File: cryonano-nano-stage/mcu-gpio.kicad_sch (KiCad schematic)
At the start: 18 parts, among them U11 STM32H753ZITx

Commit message: sch improved
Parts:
- removed C14: 4.7u, Capacitor_SMD:C_0603_1608Metric, symbol Device:C_Small
- removed C15, C43, C44, C45, C46, C47, C48, C49, C50, C53, C55: 100n, Capacitor_SMD:C_0603_1608Metric, symbol Device:C_Small
- removed C51, C52, C54: 1u, Capacitor_SMD:C_0603_1608Metric, symbol Device:C_Small
- removed C56, C57: 2.2u, Capacitor_SMD:C_0603_1608Metric, symbol Device:C_Small
- removed U11: STM32H753ZITx, Package_QFP:LQFP-144_20x20mm_P0.5mm, symbol symbols:STM32H753ZITx
- added C16, C17: 100n, Capacitor_SMD:C_0603_1608Metric, symbol Device:C_Small
- added C33, C34, C36, C37: 22pF, Capacitor_SMD:C_0603_1608Metric, symbol Device:C_Small
- added D1: PESD3V3S1UL, Diode_SMD:D_SOD-882, symbol Diode:PESD3V3S1UL
- added R35: 470R, Resistor_SMD:R_0603_1608Metric, symbol Device:R_Small
- added R36, R38, R68, R86: 10k, Resistor_SMD:R_0603_1608Metric, symbol Device:R_Small
- added SW1: BOOT, Button_Switch_THT:SW_PUSH_6mm, symbol Switch:SW_Push
- added SW2: RESET, Button_Switch_THT:SW_PUSH_6mm, symbol Switch:SW_Push
- added U11: STM32H753ZITx, Package_QFP:LQFP-144_20x20mm_P0.5mm, symbol symbols:STM32H753ZITx
- added Y2, Y4: 12.0MHz, Crystal:Crystal_SMD_3215-2Pin_3.2x1.5mm, symbol Device:Crystal
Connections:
- net VDD: now also R35.1, R38.1
- new net: R35.2, SW1.2
- new net BOOT0: C16.1, R36.1, SW1.1, U11.138 (BOOT0)
- new net CLKOUT: U11.100 (PA8)
- new net LOG_RX: U11.112 (PC11)
- new net LOG_TX: U11.111 (PC10)
- new net NRST: C17.1, D1.1 (K), SW2.1, U11.25 (NRST)
- new net PA0: U11.34 (PA0)
- new net PA15: U11.110 (PA15)
- new net PA3: U11.37 (PA3)
- new net PA4: U11.40 (PA4)
- new net PA5: U11.41 (PA5)
- new net PA6: U11.42 (PA6)
- new net PA9: R68.2, U11.101 (PA9)
- new net PB0: U11.46 (PB0)
- new net PB1: U11.47 (PB1)
- new net PB11: U11.70 (PB11)
- new net PB12: U11.73 (PB12)
- new net PB2: U11.48 (PB2)
- new net PB4: U11.134 (PB4)
- new net PB5: U11.135 (PB5)
- new net PB6: U11.136 (PB6)
- new net PB7: U11.137 (PB7)
- new net PB8: U11.139 (PB8)
- new net PB9: U11.140 (PB9)
- new net PC0: U11.26 (PC0)
- new net PC12: U11.113 (PC12)
- new net PC13: U11.7 (PC13)
- new net PC2: U11.28 (PC2_C)
- new net PC3: U11.29 (PC3_C)
- new net PC6: U11.96 (PC6)
- new net PC7: U11.97 (PC7)
- new net PC8: U11.98 (PC8)
- new net PC9: U11.99 (PC9)
- new net PD0: U11.114 (PD0)
- new net PD1: U11.115 (PD1)
- new net PD12: U11.81 (PD12)
- new net PD13: U11.82 (PD13)
- new net PD14: U11.85 (PD14)
- new net PD15: U11.86 (PD15)
- new net PD2: U11.116 (PD2)
- new net PD3: U11.117 (PD3)
- new net PD4: U11.118 (PD4)
- new net PD5: U11.119 (PD5)
- new net PD6: U11.122 (PD6)
- new net PD7: U11.123 (PD7)
- new net PD8: U11.77 (PD8)
- new net PD9: U11.78 (PD9)
- new net PDR_ON: R38.2, R86.1, U11.143 (PDR_ON)
- new net PE0: U11.141 (PE0)
- new net PE1: U11.142 (PE1)
- new net PE10: U11.63 (PE10)
- new net PE11: U11.64 (PE11)
- new net PE12: U11.65 (PE12)
- new net PE13: U11.66 (PE13)
- new net PE14: U11.67 (PE14)
- new net PE2: U11.1 (PE2)
- new net PE3: U11.2 (PE3)
- new net PE4: U11.3 (PE4)
- new net PE5: U11.4 (PE5)
- new net PE6: U11.5 (PE6)
- new net PE7: U11.58 (PE7)
- new net PE8: U11.59 (PE8)
- new net PF0: U11.10 (PF0)
- new net PF1: U11.11 (PF1)
- new net PF10: U11.22 (PF10)
- new net PF11: U11.49 (PF11)
- new net PF12: U11.50 (PF12)
- new net PF13: U11.53 (PF13)
- new net PF14: U11.54 (PF14)
- new net PF15: U11.55 (PF15)
- new net PF2: U11.12 (PF2)
- new net PF3: U11.13 (PF3)
- new net PF4: U11.14 (PF4)
- new net PF5: U11.15 (PF5)
- new net PF6: U11.18 (PF6)
- new net PF7: U11.19 (PF7)
- new net PF8: U11.20 (PF8)
- new net PF9: U11.21 (PF9)
- new net PG0: U11.56 (PG0)
- new net PG1: U11.57 (PG1)
- new net PG10: U11.125 (PG10)
- new net PG12: U11.127 (PG12)
- new net PG14: U11.129 (PG14)
- new net PG15: U11.132 (PG15)
- new net PG2: U11.87 (PG2)
- new net PG3: U11.88 (PG3)
- new net PG4: U11.89 (PG4)
- new net PG5: U11.90 (PG5)
- new net PG6: U11.91 (PG6)
- new net PG7: U11.92 (PG7)
- new net PG8: U11.93 (PG8)
- new net PG9: U11.124 (PG9)
- new net PWMOUT: U11.60 (PE9)
- new net RCC_OSC32_IN: C36.1, U11.8 (PC14), Y2.2
- new net RCC_OSC32_OUT: C37.1, U11.9 (PC15), Y2.1
- new net RCC_OSC_IN: C33.1, U11.23 (PH0), Y4.2
- new net RCC_OSC_OUT: C34.1, U11.24 (PH1), Y4.1
- new net RMII_CRS_DV: U11.43 (PA7)
- new net RMII_MDC: U11.27 (PC1)
- new net RMII_MDIO: U11.36 (PA2)
- new net RMII_REF_CLK: U11.35 (PA1)
- new net RMII_RXD0: U11.44 (PC4)
- new net RMII_RXD1: U11.45 (PC5)
- new net RMII_TXD0: U11.128 (PG13)
- new net RMII_TXD1: U11.74 (PB13)
- new net RMII_TX_EN: U11.126 (PG11)
- new net SCK: U11.69 (PB10)
- new net SDI: U11.76 (PB15)
- new net SDO/~{IRQ}: U11.75 (PB14), U11.79 (PD10)
- new net SWCLK: U11.109 (PA14)
- new net SWDIO: U11.105 (PA13)
- new net SWO: U11.133 (PB3)
- new net USB_D+: U11.104 (PA12)
- new net USB_D-: U11.103 (PA11)
- new net USB_ID: U11.102 (PA10)
- new net USB_VBUS_SENSE: R68.1
- new net VSS: C16.2, C17.2, C33.2, C34.2, C36.2, C37.2, D1.2 (A), R36.2, R86.2, SW2.2
- new net ~{CS}: U11.80 (PD11)
- new net ~{SYNC}: U11.68 (PE15)
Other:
- note added: "BOOT memory selection."
- note added: "RESET"

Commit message: pcb drc ok. 68 ohm matching pending
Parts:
- removed D1: PESD3V3S1UL, Diode_SMD:D_SOD-882, symbol Diode:PESD3V3S1UL
- added D6: ESDB3V3C-AQ, symbol symbols:ESDB3V3C-AQ
- added TP2: TEST POINT, footprints:TestPoint_THTPad_D1.3mm_Drill0.8mm, symbol Connector:TestPoint
- added TP3: 1x02 2.54mm, Connector_PinSocket_2.54mm:PinSocket_1x02_P2.54mm_Vertical, symbol Connector:Conn_01x02_Socket
- C16: Manufacturer (none) -> KEMET; Order No. (none) -> C0603C104K5RAC7411; Unit Price 10 (none) -> 2.5
- C17: Manufacturer (none) -> KEMET; Order No. (none) -> C0603C104K5RAC7411; Tolerence 10% -> (none); Unit Price 10 (none) -> 2.5
- C33, C34, C36, C37: Manufacturer (none) -> YAGEO; Manufacturer_Name SAMSUNG ELECTRO-MECHANICS -> (none); Order No. (none) -> CC0603JPNPO9BN220; Unit Price 10 (none) -> 2.3; Voltage 50V -> 16V
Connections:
- net PB11 is gone; now on net RMII_TX_EN: U11.70 (PB11)
- net PB12 is gone; now on net RMII_TXD0: U11.73 (PB12)
- net PC9 is gone; now on net CLKOUT: U11.99 (PC9)
- net PE10 is gone; now on net SDO/~{IRQ}: U11.63 (PE10)
- net PE11 is gone; now on net ~{CS}: U11.64 (PE11)
- net PE12 is gone; now on net SCK: U11.65 (PE12)
- net PE13 is gone; now on net SDO/~{IRQ}: U11.66 (PE13)
- net PE14 is gone; now on net SDI: U11.67 (PE14)
- net BOOT0: now also D6.2 (SIG2)
- net CLKOUT: no longer U11.100 (PA8)
- net NRST: now also D6.1 (SIG1)
- net PB6: now also TP3.1 (Pin_1)
- net PB7: now also TP3.2 (Pin_2)
- net RMII_TXD0: no longer U11.128 (PG13)
- net RMII_TX_EN: no longer U11.126 (PG11)
- net SCK: no longer U11.69 (PB10)
- net SDI: no longer U11.76 (PB15)
- net SDO/~{IRQ}: no longer U11.75 (PB14), U11.79 (PD10)
- net VSS: now also D6.3 (COM)
- net ~{CS}: no longer U11.80 (PD11)
- new net PA8: TP2.1, U11.100 (PA8)
- new net PB10: U11.69 (PB10)
- new net PB14: U11.75 (PB14)
- new net PB15: U11.76 (PB15)
- new net PD10: U11.79 (PD10)
- new net PD11: U11.80 (PD11)
- new net PG11: U11.126 (PG11)
- new net PG13: U11.128 (PG13)
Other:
- note added: "ESD"
- moved on the sheet: C16, C17, R35, R36, SW1, SW2

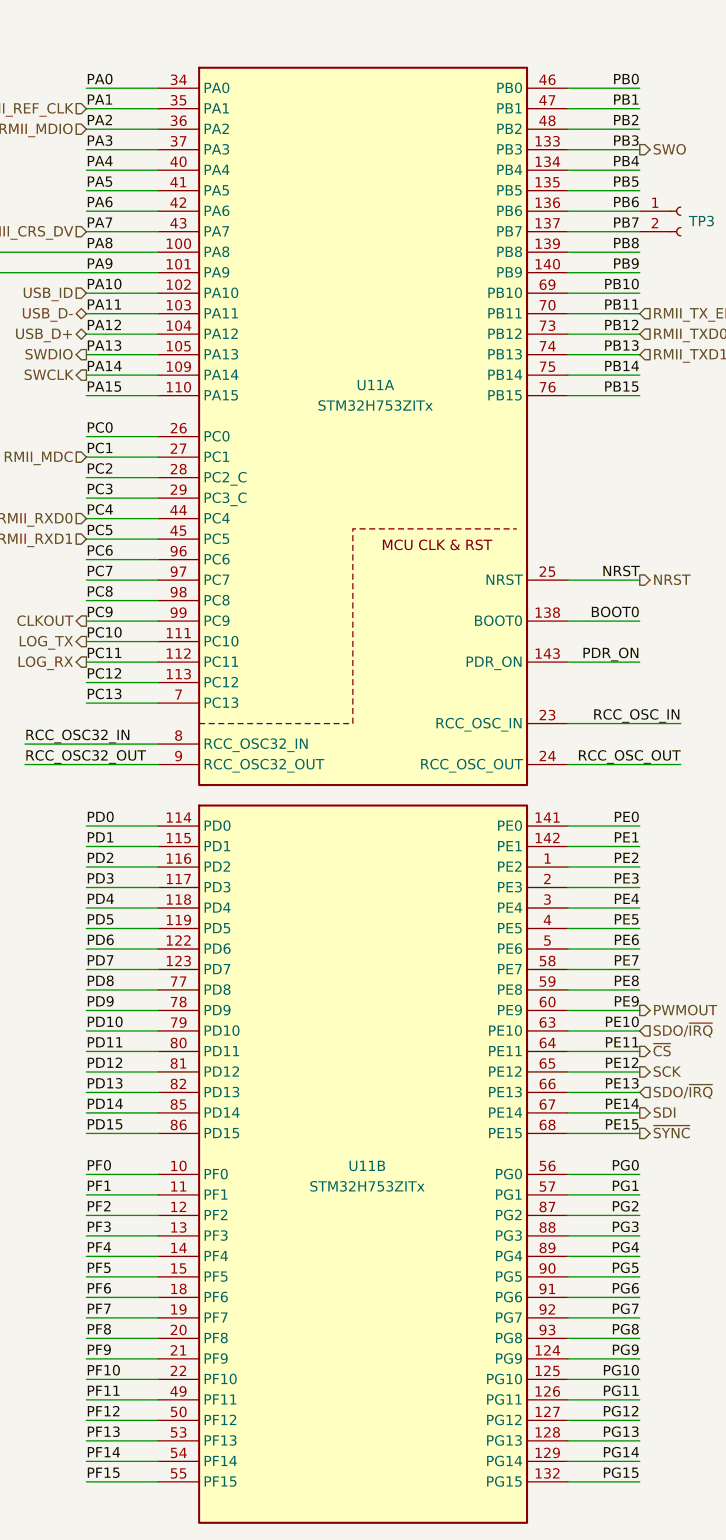
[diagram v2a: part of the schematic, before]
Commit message: drc no error, only warnings
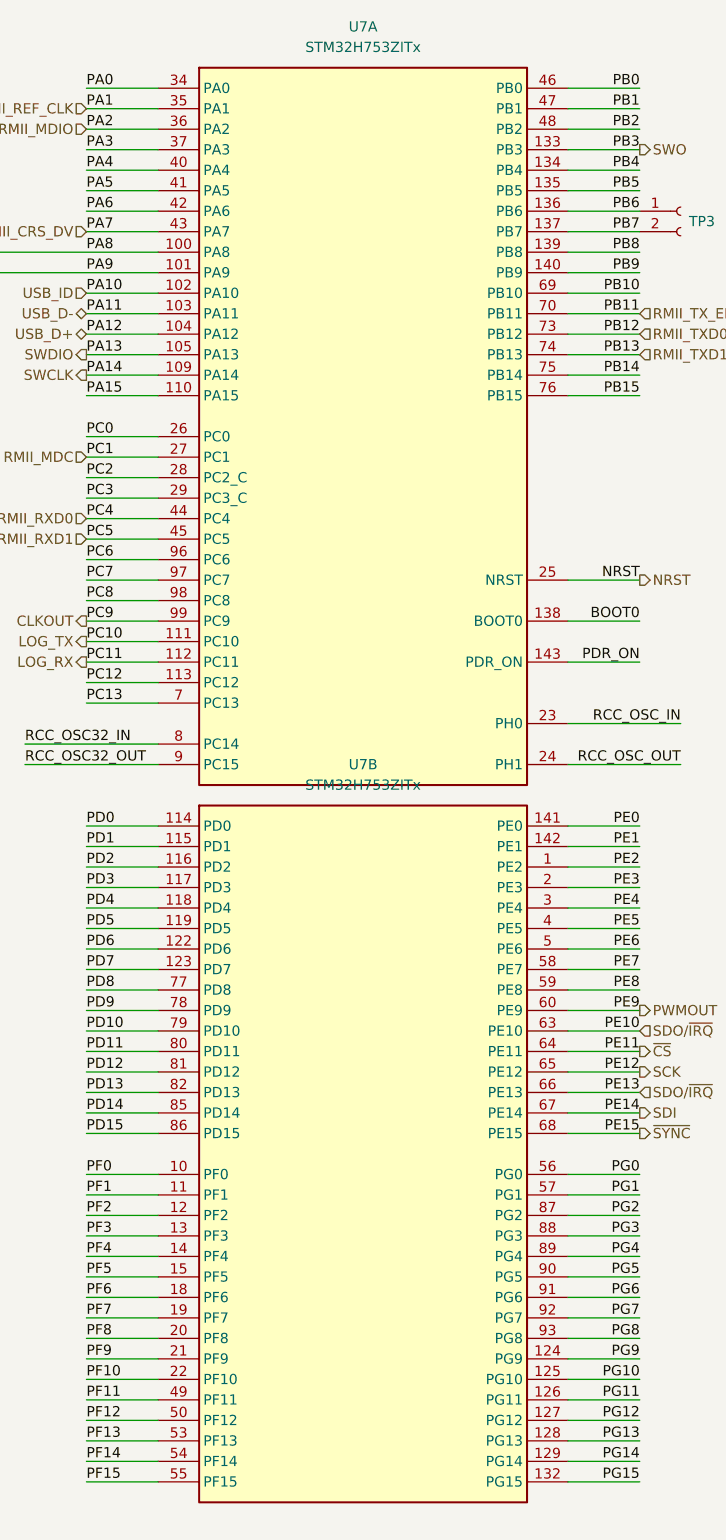
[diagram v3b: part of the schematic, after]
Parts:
- removed U11: STM32H753ZITx, Package_QFP:LQFP-144_20x20mm_P0.5mm, symbol symbols:STM32H753ZITx
- added U7: STM32H753ZITx, Package_QFP:LQFP-144_20x20mm_P0.5mm, symbol symbols:STM32H753ZITx
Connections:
- net BOOT0: now also U7.138 (BOOT0)
- net CLKOUT: now also U7.99 (PC9)
- net LOG_RX: now also U7.112 (PC11)
- net LOG_TX: now also U7.111 (PC10)
- net NRST: now also U7.25 (NRST)
- net PA0: now also U7.34 (PA0)
- net PA15: now also U7.110 (PA15)
- net PA3: now also U7.37 (PA3)
- net PA4: now also U7.40 (PA4)
- net PA5: now also U7.41 (PA5)
- net PA6: now also U7.42 (PA6)
- net PA8: now also U7.100 (PA8)
- net PA9: now also U7.101 (PA9)
- net PB0: now also U7.46 (PB0)
- net PB1: now also U7.47 (PB1)
- net PB10: now also U7.69 (PB10)
- net PB14: now also U7.75 (PB14)
- net PB15: now also U7.76 (PB15)
- net PB2: now also U7.48 (PB2)
- net PB4: now also U7.134 (PB4)
- net PB5: now also U7.135 (PB5)
- net PB6: now also U7.136 (PB6)
- net PB7: now also U7.137 (PB7)
- net PB8: now also U7.139 (PB8)
- net PB9: now also U7.140 (PB9)
- net PC0: now also U7.26 (PC0)
- net PC12: now also U7.113 (PC12)
- net PC13: now also U7.7 (PC13)
- net PC2: now also U7.28 (PC2_C)
- net PC3: now also U7.29 (PC3_C)
- net PC6: now also U7.96 (PC6)
- net PC7: now also U7.97 (PC7)
- net PC8: now also U7.98 (PC8)
- net PD0: now also U7.114 (PD0)
- net PD1: now also U7.115 (PD1)
- net PD10: now also U7.79 (PD10)
- net PD11: now also U7.80 (PD11)
- net PD12: now also U7.81 (PD12)
- net PD13: now also U7.82 (PD13)
- net PD14: now also U7.85 (PD14)
- net PD15: now also U7.86 (PD15)
- net PD2: now also U7.116 (PD2)
- net PD3: now also U7.117 (PD3)
- net PD4: now also U7.118 (PD4)
- net PD5: now also U7.119 (PD5)
- net PD6: now also U7.122 (PD6)
- net PD7: now also U7.123 (PD7)
- net PD8: now also U7.77 (PD8)
- net PD9: now also U7.78 (PD9)
- net PDR_ON: now also U7.143 (PDR_ON)
- net PE0: now also U7.141 (PE0)
- net PE1: now also U7.142 (PE1)
- net PE2: now also U7.1 (PE2)
- net PE3: now also U7.2 (PE3)
- net PE4: now also U7.3 (PE4)
- net PE5: now also U7.4 (PE5)
- net PE6: now also U7.5 (PE6)
- net PE7: now also U7.58 (PE7)
- net PE8: now also U7.59 (PE8)
- net PF0: now also U7.10 (PF0)
- net PF1: now also U7.11 (PF1)
- net PF10: now also U7.22 (PF10)
- net PF11: now also U7.49 (PF11)
- net PF12: now also U7.50 (PF12)
- net PF13: now also U7.53 (PF13)
- net PF14: now also U7.54 (PF14)
- net PF15: now also U7.55 (PF15)
- net PF2: now also U7.12 (PF2)
- net PF3: now also U7.13 (PF3)
- net PF4: now also U7.14 (PF4)
- net PF5: now also U7.15 (PF5)
- net PF6: now also U7.18 (PF6)
- net PF7: now also U7.19 (PF7)
- net PF8: now also U7.20 (PF8)
- net PF9: now also U7.21 (PF9)
- net PG0: now also U7.56 (PG0)
- net PG1: now also U7.57 (PG1)
- net PG10: now also U7.125 (PG10)
- net PG11: now also U7.126 (PG11)
- net PG12: now also U7.127 (PG12)
- net PG13: now also U7.128 (PG13)
- net PG14: now also U7.129 (PG14)
- net PG15: now also U7.132 (PG15)
- net PG2: now also U7.87 (PG2)
- net PG3: now also U7.88 (PG3)
- net PG4: now also U7.89 (PG4)
- net PG5: now also U7.90 (PG5)
- net PG6: now also U7.91 (PG6)
- net PG7: now also U7.92 (PG7)
- net PG8: now also U7.93 (PG8)
- net PG9: now also U7.124 (PG9)
- net PWMOUT: now also U7.60 (PE9)
- net RCC_OSC32_IN: now also U7.8 (PC14)
- net RCC_OSC32_OUT: now also U7.9 (PC15)
- net RCC_OSC_IN: now also U7.23 (PH0)
- net RCC_OSC_OUT: now also U7.24 (PH1)
- net RMII_CRS_DV: now also U7.43 (PA7)
- net RMII_MDC: now also U7.27 (PC1)
- net RMII_MDIO: now also U7.36 (PA2)
- net RMII_REF_CLK: now also U7.35 (PA1)
- net RMII_RXD0: now also U7.44 (PC4)
- net RMII_RXD1: now also U7.45 (PC5)
- net RMII_TXD0: now also U7.73 (PB12)
- net RMII_TXD1: now also U7.74 (PB13)
- net RMII_TX_EN: now also U7.70 (PB11)
- net SCK: now also U7.65 (PE12)
- net SDI: now also U7.67 (PE14)
- net SDO/~{IRQ}: now also U7.63 (PE10), U7.66 (PE13)
- net SWCLK: now also U7.109 (PA14)
- net SWDIO: now also U7.105 (PA13)
- net SWO: now also U7.133 (PB3)
- net USB_D+: now also U7.104 (PA12)
- net USB_D-: now also U7.103 (PA11)
- net USB_ID: now also U7.102 (PA10)
- net ~{CS}: now also U7.64 (PE11)
- net ~{SYNC}: now also U7.68 (PE15)

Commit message: complete
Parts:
- D6: footprint (none) -> Package_TO_SOT_SMD:SOT-23
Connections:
- net PA0: no longer names the net of U7.34 (PA0)
- net PA15: no longer names the net of U7.110 (PA15)
- net PA3: no longer names the net of U7.37 (PA3)
- net PA4: no longer names the net of U7.40 (PA4)
- net PA5: no longer names the net of U7.41 (PA5)
- net PA6: no longer names the net of U7.42 (PA6)
- net PA8: no longer names the net of TP2.1, U7.100 (PA8)
- net PA9: no longer names the net of R68.2, U7.101 (PA9)
- net PB0: no longer names the net of U7.46 (PB0)
- net PB1: no longer names the net of U7.47 (PB1)
- net PB10: no longer names the net of U7.69 (PB10)
- net PB14: no longer names the net of U7.75 (PB14)
- net PB15: no longer names the net of U7.76 (PB15)
- net PB2: no longer names the net of U7.48 (PB2)
- net PB4: no longer names the net of U7.134 (PB4)
- net PB5: no longer names the net of U7.135 (PB5)
- net PB6: no longer names the net of TP3.1 (Pin_1), U7.136 (PB6)
- net PB7: no longer names the net of TP3.2 (Pin_2), U7.137 (PB7)
- net PB8: no longer names the net of U7.139 (PB8)
- net PB9: no longer names the net of U7.140 (PB9)
- net PC0: no longer names the net of U7.26 (PC0)
- net PC12: no longer names the net of U7.113 (PC12)
- net PC13: no longer names the net of U7.7 (PC13)
- net PC2: no longer names the net of U7.28 (PC2_C)
- net PC3: no longer names the net of U7.29 (PC3_C)
- net PC6: no longer names the net of U7.96 (PC6)
- net PC7: no longer names the net of U7.97 (PC7)
- net PC8: no longer names the net of U7.98 (PC8)
- net PD0: no longer names the net of U7.114 (PD0)
- net PD1: no longer names the net of U7.115 (PD1)
- net PD10: no longer names the net of U7.79 (PD10)
- net PD11: no longer names the net of U7.80 (PD11)
- net PD12: no longer names the net of U7.81 (PD12)
- net PD13: no longer names the net of U7.82 (PD13)
- net PD14: no longer names the net of U7.85 (PD14)
- net PD15: no longer names the net of U7.86 (PD15)
- net PD2: no longer names the net of U7.116 (PD2)
- net PD3: no longer names the net of U7.117 (PD3)
- net PD4: no longer names the net of U7.118 (PD4)
- net PD5: no longer names the net of U7.119 (PD5)
- net PD6: no longer names the net of U7.122 (PD6)
- net PD7: no longer names the net of U7.123 (PD7)
- net PD8: no longer names the net of U7.77 (PD8)
- net PD9: no longer names the net of U7.78 (PD9)
- net PE0: no longer names the net of U7.141 (PE0)
- net PE1: no longer names the net of U7.142 (PE1)
- net PE2: no longer names the net of U7.1 (PE2)
- net PE3: no longer names the net of U7.2 (PE3)
- net PE4: no longer names the net of U7.3 (PE4)
- net PE5: no longer names the net of U7.4 (PE5)
- net PE6: no longer names the net of U7.5 (PE6)
- net PE7: no longer names the net of U7.58 (PE7)
- net PE8: no longer names the net of U7.59 (PE8)
- net PF0: no longer names the net of U7.10 (PF0)
- net PF1: no longer names the net of U7.11 (PF1)
- net PF10: no longer names the net of U7.22 (PF10)
- net PF11: no longer names the net of U7.49 (PF11)
- net PF12: no longer names the net of U7.50 (PF12)
- net PF13: no longer names the net of U7.53 (PF13)
- net PF14: no longer names the net of U7.54 (PF14)
- net PF15: no longer names the net of U7.55 (PF15)
- net PF2: no longer names the net of U7.12 (PF2)
- net PF3: no longer names the net of U7.13 (PF3)
- net PF4: no longer names the net of U7.14 (PF4)
- net PF5: no longer names the net of U7.15 (PF5)
- net PF6: no longer names the net of U7.18 (PF6)
- net PF7: no longer names the net of U7.19 (PF7)
- net PF8: no longer names the net of U7.20 (PF8)
- net PF9: no longer names the net of U7.21 (PF9)
- net PG0: no longer names the net of U7.56 (PG0)
- net PG1: no longer names the net of U7.57 (PG1)
- net PG10: no longer names the net of U7.125 (PG10)
- net PG11: no longer names the net of U7.126 (PG11)
- net PG12: no longer names the net of U7.127 (PG12)
- net PG13: no longer names the net of U7.128 (PG13)
- net PG14: no longer names the net of U7.129 (PG14)
- net PG15: no longer names the net of U7.132 (PG15)
- net PG2: no longer names the net of U7.87 (PG2)
- net PG3: no longer names the net of U7.88 (PG3)
- net PG4: no longer names the net of U7.89 (PG4)
- net PG5: no longer names the net of U7.90 (PG5)
- net PG6: no longer names the net of U7.91 (PG6)
- net PG7: no longer names the net of U7.92 (PG7)
- net PG8: no longer names the net of U7.93 (PG8)
- net PG9: no longer names the net of U7.124 (PG9)
- no-connect marks 0 -> 81

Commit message: bom adjusted
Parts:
- removed Y4: 12.0MHz, Crystal:Crystal_SMD_3215-2Pin_3.2x1.5mm, symbol Device:Crystal
- added Y1: 12MHz, Crystal:Crystal_SMD_2520-4Pin_2.5x2.0mm, symbol symbols:RH100-12.000-18-2030-EXT-TR
- C33, C34: value 22pF -> 33pF; Manufacturer YAGEO -> (none); Order No. CC0603JPNPO9BN220 -> (none); Unit Price 10 2.3 -> (none)
- C36, C37: value 22pF -> 8p; Order No. CC0603JPNPO9BN220 -> CC0603DRNPO9BN8R0; Unit Price 10 2.3 -> 4
- D6: Order No. (none) -> ESDB3V3C-AQ
- R35, R36, R38, R68, R86: Order No. (none) -> 0603/120mW
- SW1, SW2: Order No. (none) -> 6mm, 4pin
- TP2: value TEST POINT -> 1x01, 2.54; Order No. (none) -> N.A.
- TP3: value 1x02 2.54mm -> 1x02, 2.54; Order No. (none) -> N.A.
- U7: Order No. (none) -> STM32H753ZITx
- Y2: value 12.0MHz -> 32.768kHz; Order No. (none) -> ST3215FB32768B0HPWH1
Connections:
- net RCC_OSC_IN: now also Y1.3
- net RCC_OSC_OUT: now also Y1.1
- net VSS: now also Y1.2 (G), Y1.4 (G)

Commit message: drc ok. chip level review pending
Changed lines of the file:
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@@
 		(in_pos_files yes)
 		(dnp no)
-		(fields_autoplaced yes)
 		(property "Reference" "U7"
-			(at 144.78 8.89 0)
+			(at 144.78 54.864 0)
 			(show_name no)
 			(do_not_autoplace no)
@@
 		)
 		(property "Value" "STM32H753ZITx"
-			(at 144.78 11.43 0)
+			(at 144.78 57.404 0)
 			(show_name no)
 			(do_not_autoplace no)
@@
 		(in_pos_files yes)
 		(dnp no)
-		(fields_autoplaced yes)
 		(property "Reference" "U7"
-			(at 144.78 100.33 0)
+			(at 144.78 146.304 0)
 			(show_name no)
 			(do_not_autoplace no)
@@
 		)
 		(property "Value" "STM32H753ZITx"
-			(at 144.78 102.87 0)
-			(show_name no)
-			(do_not_autoplace no)
+			(at 144.78 148.844 0)
+			(show_name no)
+			(do_not_autoplace no)

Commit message: sch reviewed
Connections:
- net SCL: now reaches TP3.1 (Pin_1), U7.136 (PB6)
- net SDA: now reaches TP3.2 (Pin_2), U7.137 (PB7)
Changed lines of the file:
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@@
+		)
+	)
+	(label "SCL"
+		(at 173.99 31.75 0)
+		(effects
+			(font
+				(size 1.27 1.27)
+			)
+			(justify left bottom)
 		)
 	)
@@
 		)
 	)
+	(label "SDA"
+		(at 173.99 34.29 0)
+		(effects
+			(font
+				(size 1.27 1.27)
+			)
+			(justify left bottom)
+		)
+	)

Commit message: release candidate
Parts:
- C33, C34: Order No. (none) -> 0603, C0G/NP0/X7R; Source in.element14.com -> (none)
- C36, C37: Source in.element14.com -> (none)
- R35, R36, R38, R68, R86: Order No. 0603/120mW -> 0603, 120mW
- TP2: Comment USB SOF -> (none); Source N.A -> (none)
- TP3: Comment I2C TP -> (none)
